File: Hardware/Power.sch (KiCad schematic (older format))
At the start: 8 parts, among them U3 AAT1217

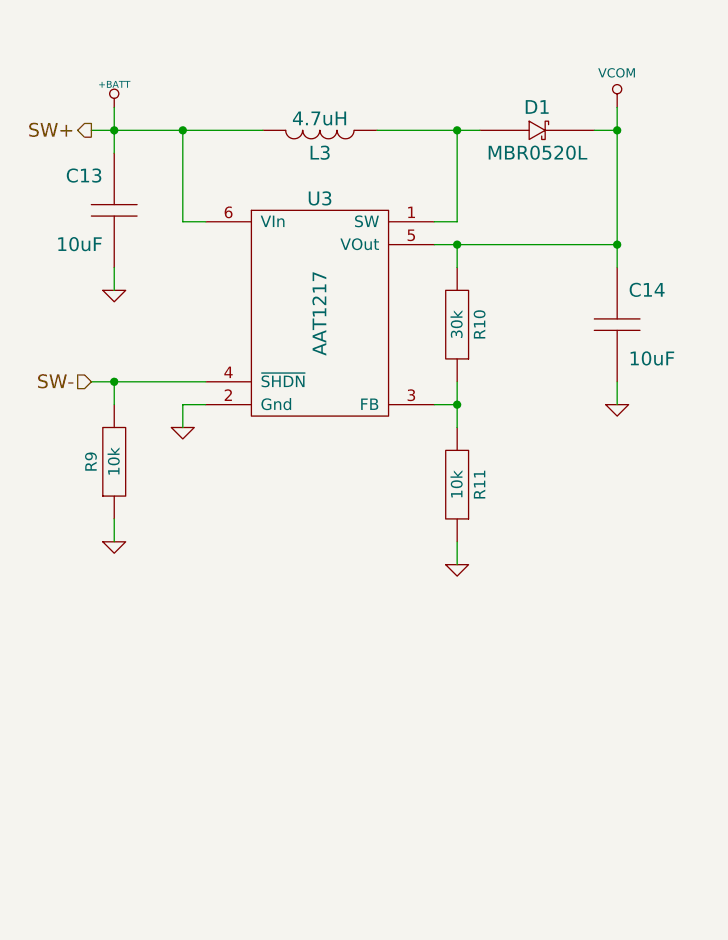
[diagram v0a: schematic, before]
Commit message: 3v3 regulator schematic and rough layout
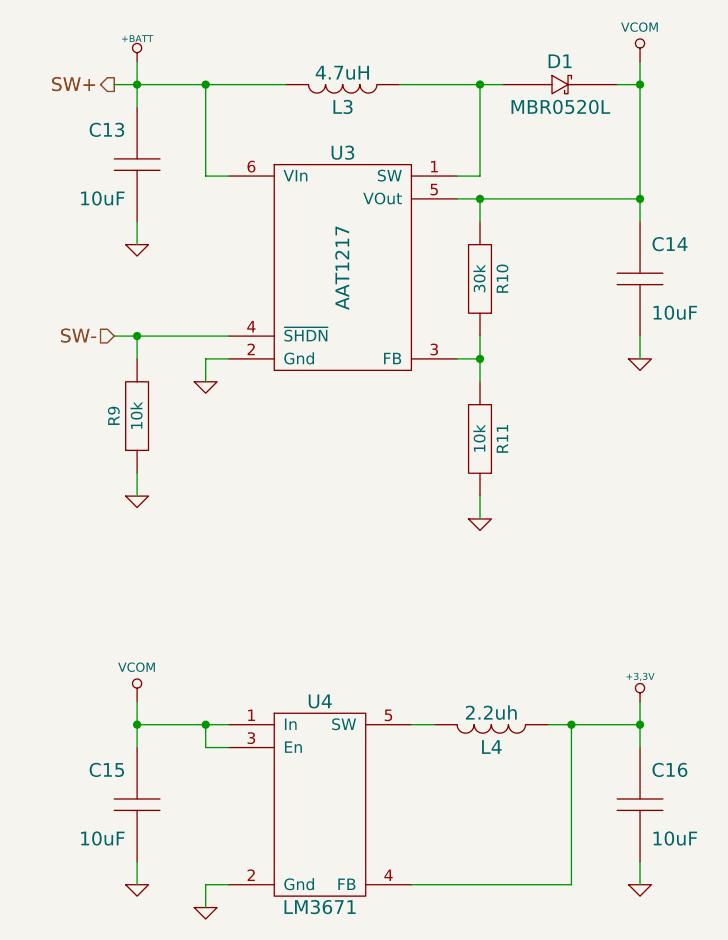
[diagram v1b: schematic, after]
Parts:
- added C15, C16: 10uF, ~, symbol C
- added L4: 2.2uh, ~, symbol L
- added U4: LM3671, symbol LM3671
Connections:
- net GND: now also C15.2, C16.2, U4.2 (Gnd)
- net VCOM: now also C15.1, U4.1 (In), U4.3 (En)
- new net: L4.1, U4.5 (SW)
- new net +3.3V: C16.1, L4.2, U4.4 (FB)
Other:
- moved on the sheet: C13, C14, D1, L3, R10, R11, R9, U3

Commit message: Add charger and batteries to schematic and board
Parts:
- added B1: 3.7v, ~, symbol BATTERY
- added B2: BATTERY, ~, symbol BATTERY
- added C17, C18, C19: 10uF, ~, symbol C
- added R12, R13, R18, R19: R, ~, symbol R
- added R14, R15, R16, R17, R20, R21, R22: 10k, ~, symbol R
- added TH1: 10k, ~, symbol THERMISTOR
- added U5: MCP73871, ~, symbol MCP73871
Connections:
- net labels added: +5V, +5VP, CE, PG, PROG2, SEL, STAT1, STAT2, ~TE
- net labels removed: VCOM
- wire segments 34 -> 92
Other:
- moved on the sheet: C13, C14, C15, C16, D1, L3, L4, R10, R11, R9, U3, U4
